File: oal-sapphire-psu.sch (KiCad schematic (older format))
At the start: 35 parts, among them P1 IEC, P2 LINE, P3 NEUTRAL, P4 PRIMARY_4, P5 PRIMARY_5, P6 SWITCHED_LINE, P7 OUTPUT, T1 TALEMA-25VA/12V, X1 MOUNTING_HOLE, X2 MOUNTING_HOLE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

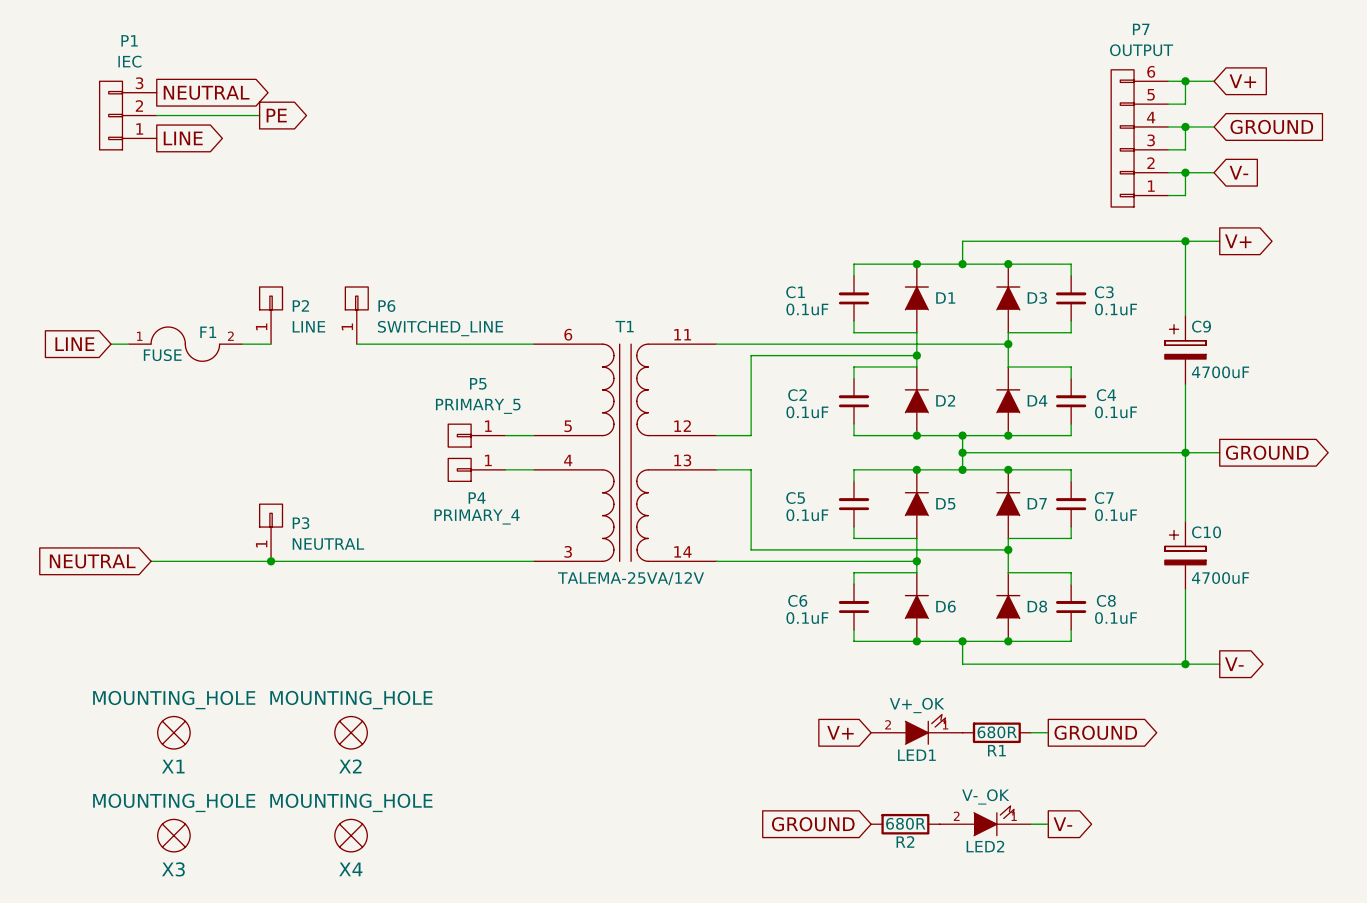
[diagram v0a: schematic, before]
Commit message: simplified 120v only layout
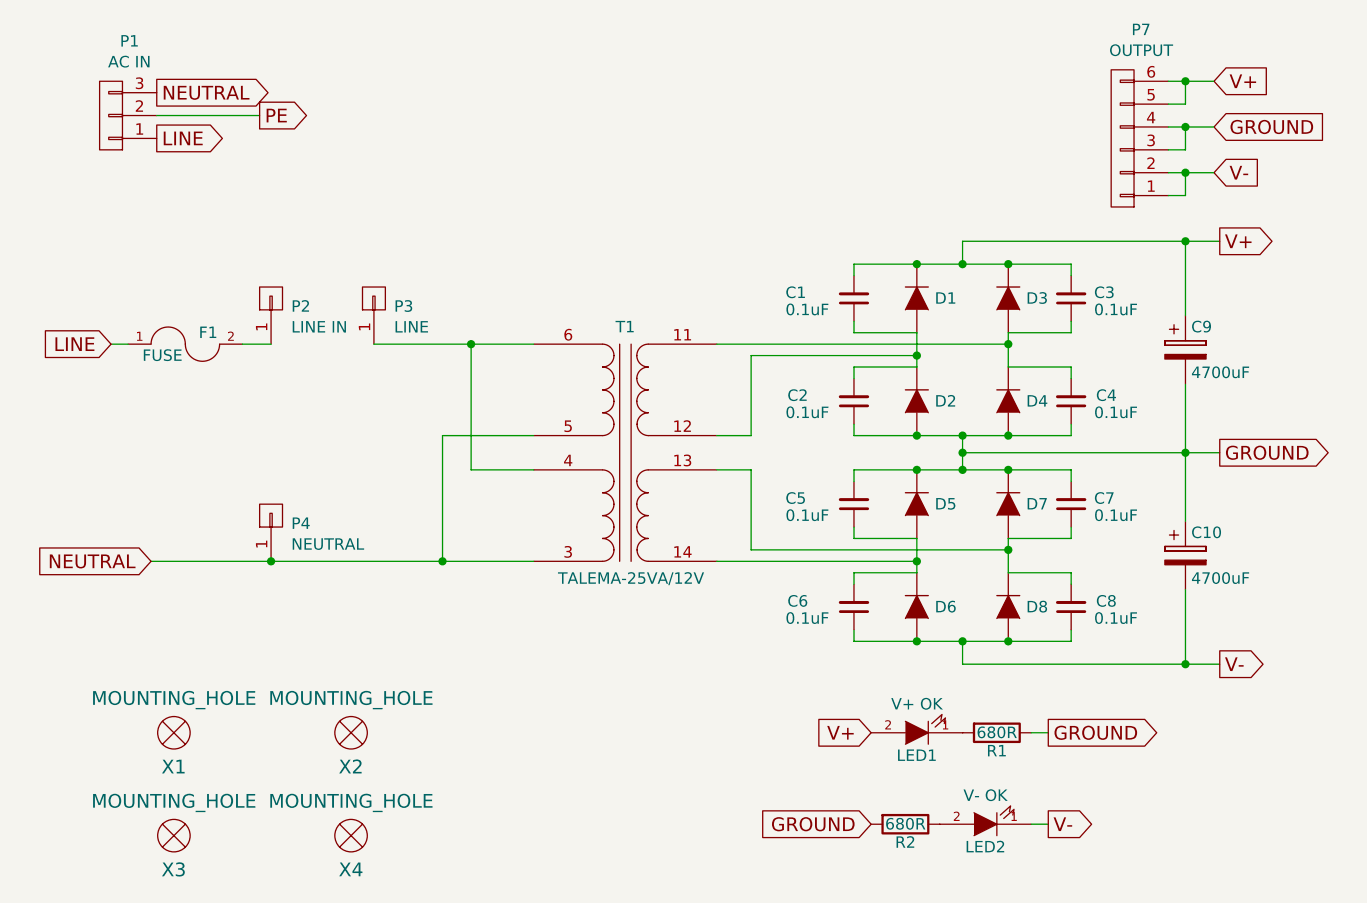
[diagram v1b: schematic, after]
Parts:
- removed P4: PRIMARY_4, ose-audio-labs:FASTON_TAB, symbol CONN_01X01
- removed P5: PRIMARY_5, ose-audio-labs:FASTON_TAB, symbol CONN_01X01
- LED1: value V+_OK -> V+ OK
- LED2: value V-_OK -> V- OK
- P1: value IEC -> AC IN
- P2: value LINE -> LINE IN
- P3: renamed from P6; value SWITCHED_LINE -> LINE
- renumbered P3 to P4
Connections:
- net NEUTRAL: now also T1.5 (PRIMARY1-NODOT)
- net at T1.4 (PRIMARY2-DOT): now also P3.1 (P1), T1.6 (PRIMARY1-DOT)
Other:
- moved on the sheet: P3
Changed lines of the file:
@@
 P 6800 5175
 F 0 "LED1" H 6800 5275 50  0000 C CNN
-F 1 "V+_OK" H 6800 5050 50  0000 C CNN
+F 1 "V+ OK" H 6800 5050 50  0000 C CNN
 F 2 "LEDs:LED_0805" H 6800 5175 50  0001 C CNN
 F 3 "" H 6800 5175 50  0000 C CNN
@@
 P 7100 5575
 F 0 "LED2" H 7100 5675 50  0000 C CNN
-F 1 "V-_OK" H 7100 5450 50  0000 C CNN
+F 1 "V- OK" H 7100 5450 50  0000 C CNN
 F 2 "LEDs:LED_0805" H 7100 5575 50  0001 C CNN
 F 3 "" H 7100 5575 50  0000 C CNN
@@
 P 3275 2475
 F 0 "P1" H 3194 2150 50  0000 C CNN
-F 1 "IEC" H 3194 2241 50  0000 C CNN
+F 1 "AC IN" H 3194 2241 50  0000 C CNN
 F 2 "ose-audio-labs:schurter_gsp1" H 3275 2475 50  0001 C CNN
 F 3 "" H 3275 2475 50  0000 C CNN
@@
 	3450 4425 5125 4425
 Wire Wire Line
-	5000 4025 5125 4025
-Wire Wire Line
-	5125 3875 5000 3875
-Wire Wire Line
-	4350 3475 5125 3475
+	4850 4025 5125 4025
+Wire Wire Line
+	4725 3875 5125 3875
+Wire Wire Line
+	4425 3475 5125 3475
 Wire Wire Line
 	3850 3475 3975 3475
@@
 P 3975 3275
 F 0 "P2" V 3940 3187 50  0000 R CNN
-F 1 "LINE" V 3849 3187 50  0000 R CNN
+F 1 "LINE IN" V 3849 3187 50  0000 R CNN
 F 2 "ose-audio-labs:FASTON_TAB" H 3975 3275 50  0001 C CNN
 F 3 "" H 3975 3275 50  0000 C CNN
@@
 $EndComp
 $Comp
-L CONN_01X01 P6
+L CONN_01X01 P3
 U 1 1 57A58547
-P 4350 3275
-F 0 "P6" V 4315 3187 50  0000 R CNN
-F 1 "SWITCHED_LINE" V 4224 3187 50  0000 R CNN
-F 2 "ose-audio-labs:FASTON_TAB" H 4350 3275 50  0001 C CNN
-F 3 "" H 4350 3275 50  0000 C CNN
-	1    4350 3275
+P 4425 3275
+F 0 "P3" V 4390 3187 50  0000 R CNN
+F 1 "LINE" V 4299 3187 50  0000 R CNN
+F 2 "ose-audio-labs:FASTON_TAB" H 4425 3275 50  0001 C CNN
+F 3 "" H 4425 3275 50  0000 C CNN
+	1    4425 3275
 	0    -1   -1   0
 $EndComp
 $Comp
-L CONN_01X01 P3
+L CONN_01X01 P4
 U 1 1 57A58A4F
 P 3975 4225
-F 0 "P3" V 3940 4137 50  0000 R CNN
+F 0 "P4" V 3940 4137 50  0000 R CNN
 F 1 "NEUTRAL" V 3849 4137 50  0000 R CNN
 F 2 "ose-audio-labs:FASTON_TAB" H 3975 4225 50  0001 C CNN
@@
 	0    -1   -1   0
 $EndComp
-$Comp
-L CONN_01X01 P5
-U 1 1 57A58B97
-P 4800 3875
-F 0 "P5" H 4719 3650 50  0000 C CNN
-F 1 "PRIMARY_5" H 4719 3741 50  0000 C CNN
-F 2 "ose-audio-labs:FASTON_TAB" H 4800 3875 50  0001 C CNN
-F 3 "" H 4800 3875 50  0000 C CNN
-	1    4800 3875
-	-1   0    0    1
-$EndComp
-$Comp
-L CONN_01X01 P4
-U 1 1 57A58D71
-P 4800 4025
-F 0 "P4" H 4725 4150 50  0000 C CNN
-F 1 "PRIMARY_4" H 4725 4225 50  0000 C CNN
-F 2 "ose-audio-labs:FASTON_TAB" H 4800 4025 50  0001 C CNN
-F 3 "" H 4800 4025 50  0000 C CNN
-	1    4800 4025
-	-1   0    0    1
-$EndComp
 Connection ~ 3975 4425
 Wire Wire Line
@@
 Wire Wire Line
 	6075 4025 5925 4025
+Wire Wire Line
+	4725 3875 4725 4425
+Connection ~ 4725 4425
+Wire Wire Line
+	4850 4025 4850 3475
+Connection ~ 4850 3475
 $EndSCHEMATC
